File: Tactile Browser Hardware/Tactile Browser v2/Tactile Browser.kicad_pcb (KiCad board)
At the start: 4 copper layers, 74.5 x 110.2 mm, 133 parts, among them SW1 SW_Push, SW10 SW_Push, SW11 SW_Push, SW12 SW_Push, SW13 SW_Push, SW14 SW_Push, SW15 SW_Push, SW16 SW_Push, SW17 SW_Push, SW18 SW_Push, SW2 SW_Push, SW3 SW_Push, SW4 SW_Push, SW5 SW_Push, SW6 SW_Push, SW7 SW_Push, SW8 SW_Push, SW9 SW_Push

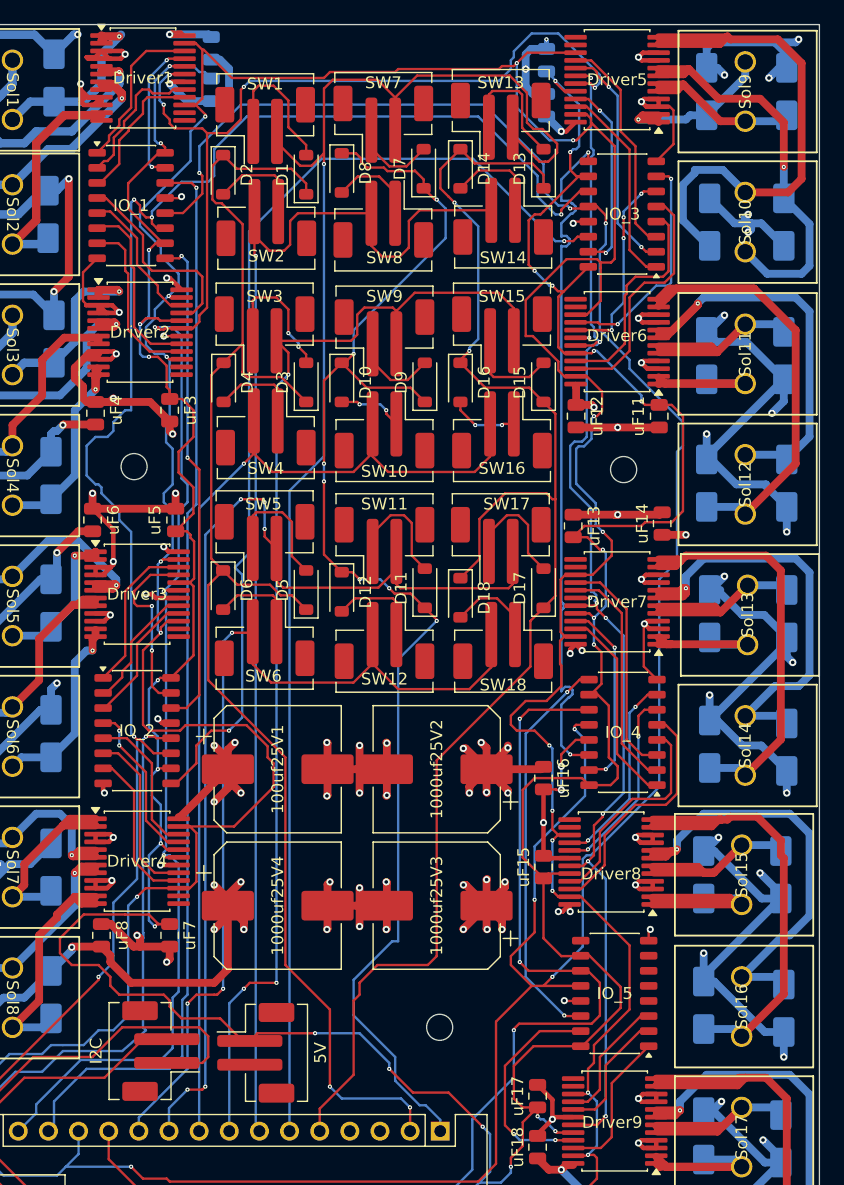
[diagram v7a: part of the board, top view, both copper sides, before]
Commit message: prepped pcb for assembly
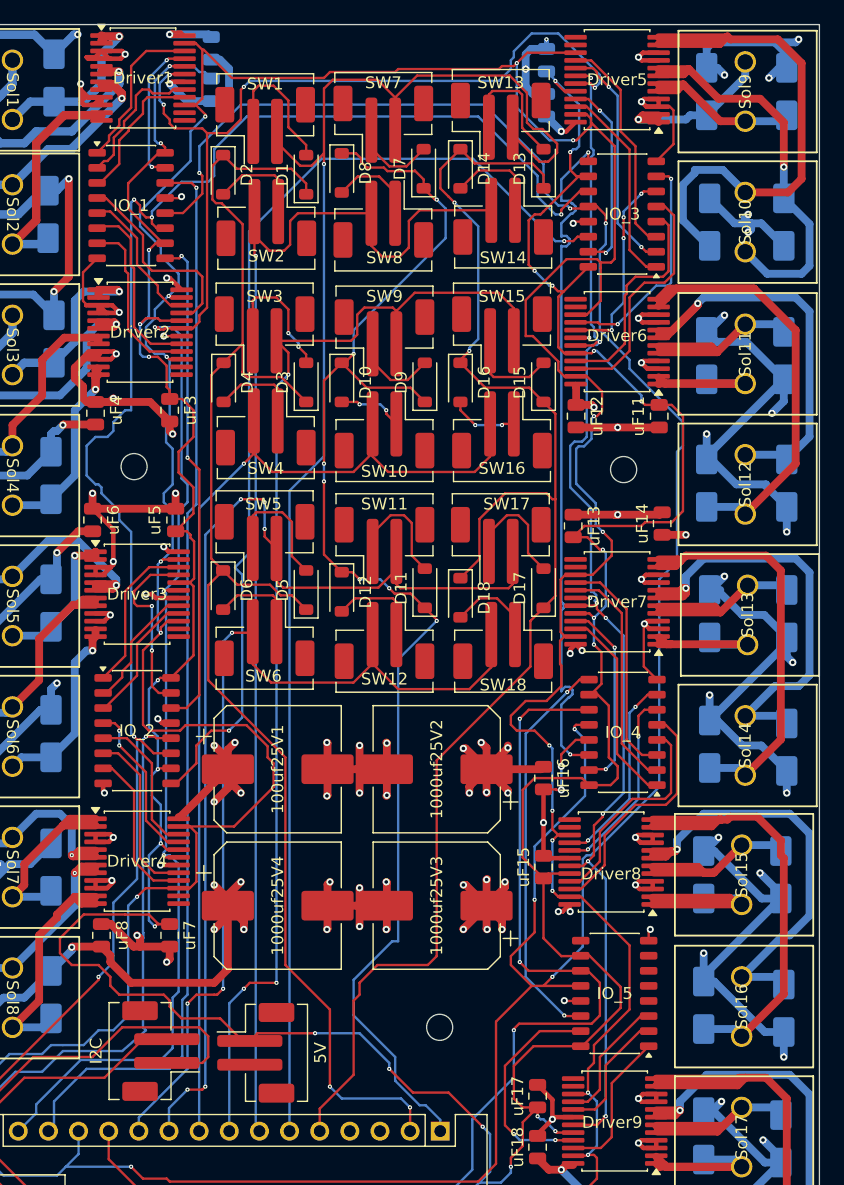
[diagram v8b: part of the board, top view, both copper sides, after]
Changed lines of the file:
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@@
 			(outputformat 1)
 			(mirror no)
-			(drillshape 1)
+			(drillshape 0)
 			(scaleselection 1)
-			(outputdirectory "")
+			(outputdirectory "gerbers/")
 		)
 	)
@@
 			(roundrect_rratio 0.25)
 			(net 3 "12V")
-			(pinfunction "VM2")
+			(pinfunction "VM3")
 			(pintype "power_in")
 		)
@@
 			(roundrect_rratio 0.25)
 			(net 3 "12V")
-			(pinfunction "VM3")
+			(pinfunction "VM1")
 			(pintype "power_in")
 		)
@@
 			(roundrect_rratio 0.25)
 			(net 3 "12V")
-			(pinfunction "VM2")
+			(pinfunction "VM3")
 			(pintype "power_in")
 		)
@@
 		(start 52.5 38)
 		(end 52.4636 37.9636)
-		(width 0.7112)
+		(width 0.6604)
 		(layer "F.Cu")
 		(net 48)
 	)
 	(via
-		(at 52.5 38)
-		(size 0.3556)
-		(drill 0.1524)
+		(at 52.4636 37.9636)
+		(size 0.600202)
+		(drill 0.299974)
 		(layers "F.Cu" "B.Cu")
 		(net 48)
@@
 	(via
 		(at 52.719128 40.219128)
-		(size 0.3556)
-		(drill 0.1524)
+		(size 0.600202)
+		(drill 0.299974)
 		(layers "F.Cu" "B.Cu")
 		(net 49)
@@
 	(via
 		(at 52.5 35)
-		(size 0.3556)
-		(drill 0.1524)
+		(size 0.600202)
+		(drill 0.299974)
 		(layers "F.Cu" "B.Cu")
 		(net 53)
@@
 	)
 	(segment
-		(start 52.5 35)
-		(end 52.6434 34.8566)
-		(width 0.7112)
-		(layer "B.Cu")
-		(net 53)
-	)
-	(segment
 		(start 52.5 42)
 		(end 52.5 42.5)
@@
 	(via
 		(at 52.25 59.25)
-		(size 0.3556)
-		(drill 0.1524)
+		(size 0.600202)
+		(drill 0.299974)
 		(layers "F.Cu" "B.Cu")
 		(net 55)
@@
 	(via
 		(at 52.5 56.5)
-		(size 0.3556)
-		(drill 0.1524)
+		(size 0.600202)
+		(drill 0.299974)
 		(layers "F.Cu" "B.Cu")
 		(net 59)
@@
 	(via
 		(at 50.5 64.75)
-		(size 0.3556)
-		(drill 0.1524)
+		(size 0.600202)
+		(drill 0.299974)
 		(layers "F.Cu" "B.Cu")
 		(net 61)
@@
 	(via
 		(at 48.75 78.75)
-		(size 0.3556)
-		(drill 0.1524)
+		(size 0.600202)
+		(drill 0.299974)
 		(layers "F.Cu" "B.Cu")
 		(net 65)
@@
 	(via
 		(at 52.25 81.25)
-		(size 0.3556)
-		(drill 0.1524)
+		(size 0.600202)
+		(drill 0.299974)
 		(layers "F.Cu" "B.Cu")
 		(net 66)
@@
 	(via
 		(at 50.25 86.75)
-		(size 0.3556)
-		(drill 0.1524)
+		(size 0.600202)
+		(drill 0.299974)
 		(layers "F.Cu" "B.Cu")
 		(net 67)
@@
 	(via
 		(at 96.25 42)
-		(size 0.3556)
-		(drill 0.1524)
+		(size 0.600202)
+		(drill 0.299974)
 		(layers "F.Cu" "B.Cu")
 		(net 79)
@@
 	(via
 		(at 108.5 46)
-		(size 0.3556)
-		(drill 0.1524)
+		(size 0.600202)
+		(drill 0.299974)
 		(layers "F.Cu" "B.Cu")
 		(net 80)
@@
 	(via
 		(at 101.25 57.5)
-		(size 0.3556)
-		(drill 0.1524)
+		(size 0.600202)
+		(drill 0.299974)
 		(layers "F.Cu" "B.Cu")
 		(net 90)
@@
 	(via
 		(at 100.25 81.5)
-		(size 0.3556)
-		(drill 0.1524)
+		(size 0.600202)
+		(drill 0.299974)
 		(layers "F.Cu" "B.Cu")
 		(net 96)
@@
 	(via
 		(at 99.5 103.5)
-		(size 0.3556)
-		(drill 0.1524)
+		(size 0.600202)
+		(drill 0.299974)
 		(layers "F.Cu" "B.Cu")
 		(net 107)
@@
 	(via
 		(at 99.75 125.5)
-		(size 0.3556)
-		(drill 0.1524)
+		(size 0.600202)
+		(drill 0.299974)
 		(layers "F.Cu" "B.Cu")
 		(net 115)
